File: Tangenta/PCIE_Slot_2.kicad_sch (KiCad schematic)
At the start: 4 parts, among them J10 1-2199230-5

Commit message: PCIe schematic continued...
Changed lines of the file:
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@@
 (kicad_sch (version 20230121) (generator eeschema)
   (paper "A4")
+  (wire (pts (xy 31.75 30.48) (xy 15.24 30.48))
+    (stroke (width 0) (type default))
+  )
+  (wire (pts (xy 31.75 20.32) (xy 15.24 20.32))
+    (stroke (width 0) (type default))
+  )
+  (wire (pts (xy 31.75 35.56) (xy 15.24 35.56))
+    (stroke (width 0) (type default))
+  )
+  (wire (pts (xy 31.75 26.67) (xy 15.24 26.67))
+    (stroke (width 0) (type default))
+  )
+  (wire (pts (xy 31.75 38.1) (xy 15.24 38.1))
+    (stroke (width 0) (type default))
+  )
+  (wire (pts (xy 31.75 24.13) (xy 15.24 24.13))
+    (stroke (width 0) (type default))
+  )
+  (wire (pts (xy 31.75 33.02) (xy 15.24 33.02))
+    (stroke (width 0) (type default))
+  )
+  (wire (pts (xy 15.24 17.78) (xy 31.75 17.78))
+    (stroke (width 0) (type default))
+  )
+  (label "PCIE2_RX_N" (at 15.24 33.02 0) (fields_autoplaced)
+    (effects (font (size 1.27 1.27)) (justify left bottom))
+  )
+  (label "PCIE2_PRSNT" (at 15.24 17.78 0) (fields_autoplaced)
+    (effects (font (size 1.27 1.27)) (justify left bottom))
+  )
+  (label "PCIE2_CLK_P" (at 15.24 24.13 0) (fields_autoplaced)
+    (effects (font (size 1.27 1.27)) (justify left bottom))
+  )
+  (label "PCIE2_TX_N" (at 15.24 38.1 0) (fields_autoplaced)
+    (effects (font (size 1.27 1.27)) (justify left bottom))
+  )
+  (label "PCIE2_PERST" (at 15.24 20.32 0) (fields_autoplaced)
+    (effects (font (size 1.27 1.27)) (justify left bottom))
+  )
+  (label "PCIE2_TX_P" (at 15.24 35.56 0) (fields_autoplaced)
+    (effects (font (size 1.27 1.27)) (justify left bottom))
+  )
+  (label "PCIE2_CLK_N" (at 15.24 26.67 0) (fields_autoplaced)
+    (effects (font (size 1.27 1.27)) (justify left bottom))
+  )
+  (label "PCIE2_RX_P" (at 15.24 30.48 0) (fields_autoplaced)
+    (effects (font (size 1.27 1.27)) (justify left bottom))
+  )
+  (hierarchical_label "PCIE2_CLK_P" (shape input) (at 31.75 24.13 0) (fields_autoplaced)
+    (effects (font (size 1.27 1.27)) (justify left))
+  )
+  (hierarchical_label "PCIE2_TX_N" (shape input) (at 31.75 38.1 0) (fields_autoplaced)
+    (effects (font (size 1.27 1.27)) (justify left))
+  )
+  (hierarchical_label "PCIE2_CLK_N" (shape input) (at 31.75 26.67 0) (fields_autoplaced)
+    (effects (font (size 1.27 1.27)) (justify left))
+  )
+  (hierarchical_label "PCIE2_PRSNT" (shape input) (at 31.75 17.78 0) (fields_autoplaced)
+    (effects (font (size 1.27 1.27)) (justify left))
+  )
+  (hierarchical_label "PCIE2_RX_P" (shape input) (at 31.75 30.48 0) (fields_autoplaced)
+    (effects (font (size 1.27 1.27)) (justify left))
+  )
+  (hierarchical_label "PCIE2_RX_N" (shape input) (at 31.75 33.02 0) (fields_autoplaced)
+    (effects (font (size 1.27 1.27)) (justify left))
+  )
+  (hierarchical_label "PCIE2_TX_P" (shape input) (at 31.75 35.56 0) (fields_autoplaced)
+    (effects (font (size 1.27 1.27)) (justify left))
+  )
+  (hierarchical_label "PCIE2_PERST" (shape input) (at 31.75 20.32 0) (fields_autoplaced)
+    (effects (font (size 1.27 1.27)) (justify left))
+  )
   (symbol (lib_id "Mechanical:MountingHole") (at 168.91 104.14 0) (unit 1)
     (in_bom yes) (on_board yes) (dnp no)

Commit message: ...
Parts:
- added R2: 0R, Resistor_SMD:R_0402_1005Metric, symbol Device:R_Small_US
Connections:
- new net PCIE2_nWAKE: R2.2
- new net nWAKE: R2.1
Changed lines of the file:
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@@
 (kicad_sch (version 20230121) (generator eeschema)
   (paper "A4")
+  (wire (pts (xy 15.24 14.605) (xy 31.75 14.605))
+    (stroke (width 0) (type default))
+  )
+  (wire (pts (xy 15.24 45.72) (xy 31.75 45.72))
+    (stroke (width 0) (type default))
+  )
+  (wire (pts (xy 36.83 45.72) (xy 45.72 45.72))
+    (stroke (width 0) (type default))
+  )
   (wire (pts (xy 31.75 30.48) (xy 15.24 30.48))
     (stroke (width 0) (type default))
@@
     (stroke (width 0) (type default))
   )
+  (wire (pts (xy 31.75 41.275) (xy 15.24 41.275))
+    (stroke (width 0) (type default))
+  )
   (wire (pts (xy 31.75 38.1) (xy 15.24 38.1))
     (stroke (width 0) (type default))
@@
     (stroke (width 0) (type default))
   )
+  (label "PCIE2_nWAKE" (at 15.24 45.72 0) (fields_autoplaced)
+    (effects (font (size 1.27 1.27)) (justify left bottom))
+  )
   (label "PCIE2_RX_N" (at 15.24 33.02 0) (fields_autoplaced)
     (effects (font (size 1.27 1.27)) (justify left bottom))
   )
+  (label "12V" (at 15.24 14.605 0) (fields_autoplaced)
+    (effects (font (size 1.27 1.27)) (justify left bottom))
+  )
   (label "PCIE2_PRSNT" (at 15.24 17.78 0) (fields_autoplaced)
     (effects (font (size 1.27 1.27)) (justify left bottom))
   )
+  (label "nWAKE" (at 45.72 45.72 180) (fields_autoplaced)
+    (effects (font (size 1.27 1.27)) (justify right bottom))
+  )
   (label "PCIE2_CLK_P" (at 15.24 24.13 0) (fields_autoplaced)
     (effects (font (size 1.27 1.27)) (justify left bottom))
@@
     (effects (font (size 1.27 1.27)) (justify left bottom))
   )
+  (label "PCIE2_nWAKE" (at 15.24 41.275 0) (fields_autoplaced)
+    (effects (font (size 1.27 1.27)) (justify left bottom))
+  )
   (label "PCIE2_PERST" (at 15.24 20.32 0) (fields_autoplaced)
     (effects (font (size 1.27 1.27)) (justify left bottom))
@@
     (effects (font (size 1.27 1.27)) (justify left bottom))
   )
+  (hierarchical_label "PCIE2_nWAKE" (shape input) (at 31.75 41.275 0) (fields_autoplaced)
+    (effects (font (size 1.27 1.27)) (justify left))
+  )
   (hierarchical_label "PCIE2_CLK_P" (shape input) (at 31.75 24.13 0) (fields_autoplaced)
     (effects (font (size 1.27 1.27)) (justify left))
@@
   )
   (hierarchical_label "PCIE2_PERST" (shape input) (at 31.75 20.32 0) (fields_autoplaced)
+    (effects (font (size 1.27 1.27)) (justify left))
+  )
+  (hierarchical_label "12V" (shape input) (at 31.75 14.605 0) (fields_autoplaced)
     (effects (font (size 1.27 1.27)) (justify left))
   )
@@
         )
       )
+    )
+  )
+  (symbol (lib_id "Device:R_Small_US") (at 34.29 45.72 270) (unit 1)
+    (in_bom yes) (on_board yes) (dnp no)
+    (property "Reference" "R2" (at 28.575 44.45 90)
+      (effects (font (size 1.27 1.27)) (justify left))
+    )
+    (property "Value" "0R" (at 35.56 44.45 90)
+      (effects (font (size 1.27 1.27)) (justify left))
+    )
+    (property "Footprint" "Resistor_SMD:R_0402_1005Metric" (at 34.29 45.72 0)
+      (effects (font (size 1.27 1.27)) hide)
+    )
+    (property "Datasheet" "~" (at 34.29 45.72 0)
+      (effects (font (size 1.27 1.27)) hide)
+    )
+    (pin "1")
+    (pin "2")
+    (instances
+      (project "Tangenta"
+        (path "/358d1bcf-7599-4352-8c4d-baa18a5f09e6/8215796b-9611-4f43-bcc5-319f8414b8a6"
+          (reference "R2") (unit 1)
+        )
+        (path "/358d1bcf-7599-4352-8c4d-baa18a5f09e6/d6c05402-162e-441f-bed8-be7996260fb4"
+          (reference "R18") (unit 1)
+        )
+        (path "/358d1bcf-7599-4352-8c4d-baa18a5f09e6/b1871a4d-6a35-44e2-a9a2-9a4af684371d"
+          (reference "R26") (unit 1)
+        )
+        (path "/358d1bcf-7599-4352-8c4d-baa18a5f09e6/6a8c68b5-4a7d-449e-86f6-34ced6d1cb55"
+          (reference "R41") (unit 1)
+        )
+        (path "/358d1bcf-7599-4352-8c4d-baa18a5f09e6/db297b0b-35f2-4e86-892c-83973f1ac2db"
+          (reference "R56") (unit 1)
+        )
+        (path "/358d1bcf-7599-4352-8c4d-baa18a5f09e6/9b1f6f94-444c-4c59-8de9-290bde336856/79105fff-2111-4675-95ec-60397c562e45"
+          (reference "R62") (unit 1)
+        )
+        (path "/358d1bcf-7599-4352-8c4d-baa18a5f09e6/9b1f6f94-444c-4c59-8de9-290bde336856/90adec24-c816-45b1-84de-df0a62ed06ad"
+          (reference "R63") (unit 1)
+        )
+      )

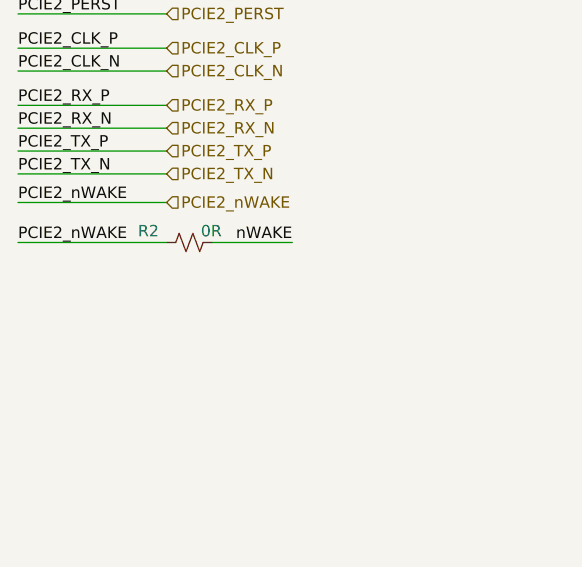
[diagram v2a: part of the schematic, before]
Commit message: PCIe switch schematic, continued...
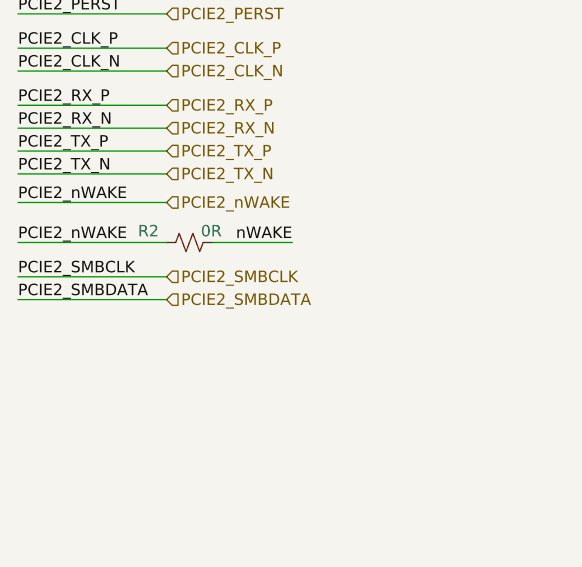
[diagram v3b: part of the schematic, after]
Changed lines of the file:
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@@
+    (stroke (width 0) (type default))
+  )
+  (wire (pts (xy 31.75 52.07) (xy 15.24 52.07))
     (stroke (width 0) (type default))
   )
@@
   )
   (wire (pts (xy 31.75 38.1) (xy 15.24 38.1))
+    (stroke (width 0) (type default))
+  )
+  (wire (pts (xy 31.75 49.53) (xy 15.24 49.53))
     (stroke (width 0) (type default))
   )
@@
     (effects (font (size 1.27 1.27)) (justify left bottom))
   )
+  (label "PCIE2_SMBCLK" (at 15.24 49.53 0) (fields_autoplaced)
+    (effects (font (size 1.27 1.27)) (justify left bottom))
+  )
   (label "PCIE2_RX_N" (at 15.24 33.02 0) (fields_autoplaced)
     (effects (font (size 1.27 1.27)) (justify left bottom))
   )
   (label "12V" (at 15.24 14.605 0) (fields_autoplaced)
+    (effects (font (size 1.27 1.27)) (justify left bottom))
+  )
+  (label "PCIE2_SMBDATA" (at 15.24 52.07 0) (fields_autoplaced)
     (effects (font (size 1.27 1.27)) (justify left bottom))
   )
@@
     (effects (font (size 1.27 1.27)) (justify left))
   )
+  (hierarchical_label "PCIE2_SMBDATA" (shape input) (at 31.75 52.07 0) (fields_autoplaced)
+    (effects (font (size 1.27 1.27)) (justify left))
+  )
   (hierarchical_label "PCIE2_CLK_P" (shape input) (at 31.75 24.13 0) (fields_autoplaced)
     (effects (font (size 1.27 1.27)) (justify left))
@@
     (effects (font (size 1.27 1.27)) (justify left))
   )
+  (hierarchical_label "PCIE2_SMBCLK" (shape input) (at 31.75 49.53 0) (fields_autoplaced)
+    (effects (font (size 1.27 1.27)) (justify left))
+  )

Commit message: ...
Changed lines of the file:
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@@
 (kicad_sch (version 20230121) (generator eeschema)
   (paper "A4")
-  (wire (pts (xy 15.24 14.605) (xy 31.75 14.605))
+  (wire (pts (xy 15.24 55.245) (xy 31.75 55.245))
     (stroke (width 0) (type default))
   )
@@
     (stroke (width 0) (type default))
   )
+  (wire (pts (xy 15.24 57.785) (xy 31.75 57.785))
+    (stroke (width 0) (type default))
+  )
   (wire (pts (xy 31.75 38.1) (xy 15.24 38.1))
     (stroke (width 0) (type default))
@@
     (stroke (width 0) (type default))
   )
+  (wire (pts (xy 15.24 62.865) (xy 31.75 62.865))
+    (stroke (width 0) (type default))
+  )
   (wire (pts (xy 31.75 33.02) (xy 15.24 33.02))
+    (stroke (width 0) (type default))
+  )
+  (wire (pts (xy 15.24 60.325) (xy 31.75 60.325))
     (stroke (width 0) (type default))
   )
   (wire (pts (xy 15.24 17.78) (xy 31.75 17.78))
     (stroke (width 0) (type default))
+  )
+  (label "GND" (at 15.24 62.865 0) (fields_autoplaced)
+    (effects (font (size 1.27 1.27)) (justify left bottom))
   )
   (label "PCIE2_nWAKE" (at 15.24 45.72 0) (fields_autoplaced)
@@
     (effects (font (size 1.27 1.27)) (justify left bottom))
   )
-  (label "12V" (at 15.24 14.605 0) (fields_autoplaced)
+  (label "12V" (at 15.24 55.245 0) (fields_autoplaced)
     (effects (font (size 1.27 1.27)) (justify left bottom))
   )
@@
   )
   (label "PCIE2_TX_N" (at 15.24 38.1 0) (fields_autoplaced)
+    (effects (font (size 1.27 1.27)) (justify left bottom))
+  )
+  (label "3V3" (at 15.24 60.325 0) (fields_autoplaced)
+    (effects (font (size 1.27 1.27)) (justify left bottom))
+  )
+  (label "3V3SB" (at 15.24 57.785 0) (fields_autoplaced)
     (effects (font (size 1.27 1.27)) (justify left bottom))
   )
@@
     (effects (font (size 1.27 1.27)) (justify left))
   )
+  (hierarchical_label "3V3" (shape input) (at 31.75 60.325 0) (fields_autoplaced)
+    (effects (font (size 1.27 1.27)) (justify left))
+  )
   (hierarchical_label "PCIE2_CLK_P" (shape input) (at 31.75 24.13 0) (fields_autoplaced)
+    (effects (font (size 1.27 1.27)) (justify left))
+  )
+  (hierarchical_label "3V3_STANDBY" (shape input) (at 31.75 57.785 0) (fields_autoplaced)
     (effects (font (size 1.27 1.27)) (justify left))
   )
@@
   )
   (hierarchical_label "PCIE2_PRSNT" (shape input) (at 31.75 17.78 0) (fields_autoplaced)
+    (effects (font (size 1.27 1.27)) (justify left))
+  )
+  (hierarchical_label "GND" (shape bidirectional) (at 31.75 62.865 0) (fields_autoplaced)
     (effects (font (size 1.27 1.27)) (justify left))
   )
@@
     (effects (font (size 1.27 1.27)) (justify left))
   )
-  (hierarchical_label "12V" (shape input) (at 31.75 14.605 0) (fields_autoplaced)
+  (hierarchical_label "12V" (shape input) (at 31.75 55.245 0) (fields_autoplaced)
     (effects (font (size 1.27 1.27)) (justify left))
   )

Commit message: ...
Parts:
- added C24 (x2): 10uF, CAP_TANTAL_A:CAP_TANTAL_A, symbol CAP_TANTAL_A:CA45-A-6_3V-47UF-K
- added R2 (x2): 47k, Resistor_SMD:R_0402_1005Metric, symbol Device:R_Small_US
- added R2 (x2): 0R, Resistor_SMD:R_0402_1005Metric, symbol Device:R_Small_US
- added TP3: TestPoint_Small, TestPoint:TestPoint_Pad_1.0x1.0mm, symbol Connector:TestPoint_Small
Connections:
- net 3V3: now also J10.2, J10.4, J10.70, J10.72, J10.74, C24.1, C24.1, R2.1, R2.1
- net GND: now also J10.11, J10.27, J10.3, J10.33, J10.39, J10.45, J10.5, J10.51, J10.57, J10.71, J10.73, J10.MP1, J10.MP2, C24.2, C24.2
- net PCIE2_CLK_N: now also J10.53
- net PCIE2_CLK_P: now also J10.55
- net PCIE2_PERST: now also J10.50
- net PCIE2_RX_N: now also J10.41
- net PCIE2_RX_P: now also J10.43
- net PCIE2_TX_N: now also J10.47
- net PCIE2_TX_P: now also J10.49
- net nWAKE: now also J10.54
- net SM_CLK: now reaches J10.40
- net SM_CLK: now also R2.2
- net SM_DAT: now reaches J10.42
- net SM_DAT: now also R2.2
- net at J10.6: now also R2.2
- net at J10.67: now also TP3.1
- net at J10.8: now also R2.2
- new net PCIE1_SMBCLK: R2.1
- new net PCIE1_SMBDATA: R2.1
- no-connect marks 0 -> 41
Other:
- moved on the sheet: H10

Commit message: Schematic improvements.
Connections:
- net PCIE1_SMBCLK is gone; now on net PCIE2_SMBCLK: R2.1
- net PCIE1_SMBDATA is gone; now on net PCIE2_SMBDATA: R2.1
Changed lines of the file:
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@@
     (effects (font (size 1.27 1.27)) (justify left bottom))
   )
-  (label "PCIE1_SMBCLK" (at 184.15 88.9 180) (fields_autoplaced)
+  (label "PCIE2_SMBCLK" (at 184.15 88.9 180) (fields_autoplaced)
     (effects (font (size 1.27 1.27)) (justify right bottom))
   )
@@
     (effects (font (size 1.27 1.27)) (justify right bottom))
   )
-  (label "PCIE1_SMBDATA" (at 184.15 91.44 180) (fields_autoplaced)
+  (label "PCIE2_SMBDATA" (at 184.15 91.44 180) (fields_autoplaced)
     (effects (font (size 1.27 1.27)) (justify right bottom))
   )

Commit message: Libraries exported from global to project.
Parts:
- C24: symbol CAP_TANTAL_A:CA45-A-6_3V-47UF-K -> CholaSymbolsPrjLib:CA45-A-6_3V-47UF-K
- H10: symbol Mechanical:MountingHole -> CholaSymbolsPrjLib:MountingHole
- J10: symbol M2_Slot:1-2199230-5 -> CholaSymbolsPrjLib:1-2199230-5
- R2: symbol Device:R_Small_US -> CholaSymbolsPrjLib:R_Small_US
- TP3: symbol Connector:TestPoint_Small -> CholaSymbolsPrjLib:TestPoint_Small
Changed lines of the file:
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@@
     (effects (font (size 1.27 1.27)) (justify left))
   )
-  (symbol (lib_id "Mechanical:MountingHole") (at 163.195 175.26 0) (unit 1)
+  (symbol (lib_id "CholaSymbolsPrjLib:MountingHole") (at 163.195 175.26 0) (unit 1)
     (in_bom yes) (on_board yes) (dnp no)
     (property "Reference" "H10" (at 165.735 175.26 0)
@@
     )
   )
-  (symbol (lib_id "Mechanical:MountingHole") (at 163.195 185.42 0) (unit 1)
+  (symbol (lib_id "CholaSymbolsPrjLib:MountingHole") (at 163.195 185.42 0) (unit 1)
     (in_bom yes) (on_board yes) (dnp no)
     (property "Reference" "H10" (at 165.735 185.42 0)
@@
     )
   )
-  (symbol (lib_id "Device:R_Small_US") (at 161.29 48.26 270) (unit 1)
+  (symbol (lib_id "CholaSymbolsPrjLib:R_Small_US") (at 161.29 48.26 270) (unit 1)
     (in_bom yes) (on_board yes) (dnp no)
     (property "Reference" "R2" (at 154.305 46.99 90)
@@
     )
   )
-  (symbol (lib_id "M2_Slot:1-2199230-5") (at 135.89 33.02 90) (mirror x) (unit 1)
+  (symbol (lib_id "CholaSymbolsPrjLib:1-2199230-5") (at 135.89 33.02 90) (mirror x) (unit 1)
     (in_bom yes) (on_board yes) (dnp no)
     (property "Reference" "J10" (at 128.27 36.83 90)
@@
     )
   )
-  (symbol (lib_id "CAP_TANTAL_A:CA45-A-6_3V-47UF-K") (at 140.97 148.59 270) (mirror x) (unit 1)
+  (symbol (lib_id "CholaSymbolsPrjLib:CA45-A-6_3V-47UF-K") (at 140.97 148.59 270) (mirror x) (unit 1)
     (in_bom yes) (on_board yes) (dnp no)
     (property "Reference" "C24" (at 148.59 147.32 90)
@@
     )
   )
-  (symbol (lib_id "Mechanical:MountingHole") (at 163.195 180.34 0) (unit 1)
+  (symbol (lib_id "CholaSymbolsPrjLib:MountingHole") (at 163.195 180.34 0) (unit 1)
     (in_bom yes) (on_board yes) (dnp no)
     (property "Reference" "H10" (at 165.735 180.34 0)
@@
     )
   )
-  (symbol (lib_id "Device:R_Small_US") (at 161.29 45.72 270) (unit 1)
+  (symbol (lib_id "CholaSymbolsPrjLib:R_Small_US") (at 161.29 45.72 270) (unit 1)
     (in_bom yes) (on_board yes) (dnp no)
     (property "Reference" "R2" (at 154.305 44.45 90)
@@
     )
   )
-  (symbol (lib_id "Device:R_Small_US") (at 163.83 91.44 270) (unit 1)
+  (symbol (lib_id "CholaSymbolsPrjLib:R_Small_US") (at 163.83 91.44 270) (unit 1)
     (in_bom yes) (on_board yes) (dnp no)
     (property "Reference" "R2" (at 156.845 90.17 90)
@@
     )
   )
-  (symbol (lib_id "CAP_TANTAL_A:CA45-A-6_3V-47UF-K") (at 130.175 148.59 270) (mirror x) (unit 1)
+  (symbol (lib_id "CholaSymbolsPrjLib:CA45-A-6_3V-47UF-K") (at 130.175 148.59 270) (mirror x) (unit 1)
     (in_bom yes) (on_board yes) (dnp no)
     (property "Reference" "C24" (at 137.795 147.32 90)
@@
     )
   )
-  (symbol (lib_id "Connector:TestPoint_Small") (at 113.03 114.3 0) (mirror y) (unit 1)
+  (symbol (lib_id "CholaSymbolsPrjLib:TestPoint_Small") (at 113.03 114.3 0) (mirror y) (unit 1)
     (in_bom yes) (on_board yes) (dnp no)
     (property "Reference" "TP3" (at 112.395 114.3 0)
@@
     )
   )
-  (symbol (lib_id "Device:R_Small_US") (at 163.83 88.9 270) (unit 1)
+  (symbol (lib_id "CholaSymbolsPrjLib:R_Small_US") (at 163.83 88.9 270) (unit 1)
     (in_bom yes) (on_board yes) (dnp no)
     (property "Reference" "R2" (at 156.845 87.63 90)
@@
     )
   )
-  (symbol (lib_id "Device:R_Small_US") (at 34.29 45.72 270) (unit 1)
+  (symbol (lib_id "CholaSymbolsPrjLib:R_Small_US") (at 34.29 45.72 270) (unit 1)
     (in_bom yes) (on_board yes) (dnp no)
     (property "Reference" "R2" (at 28.575 44.45 90)
